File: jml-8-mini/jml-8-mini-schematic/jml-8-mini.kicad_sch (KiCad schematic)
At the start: 9 parts, among them J1 Barrel_Jack, J2 Conn_01x09_Pin, SW1 SW_DPDT_x2, U1 Z80CPU, U2 28HC64, U3 60L256, U4 Z80 CTC, U5 Z80 SIO

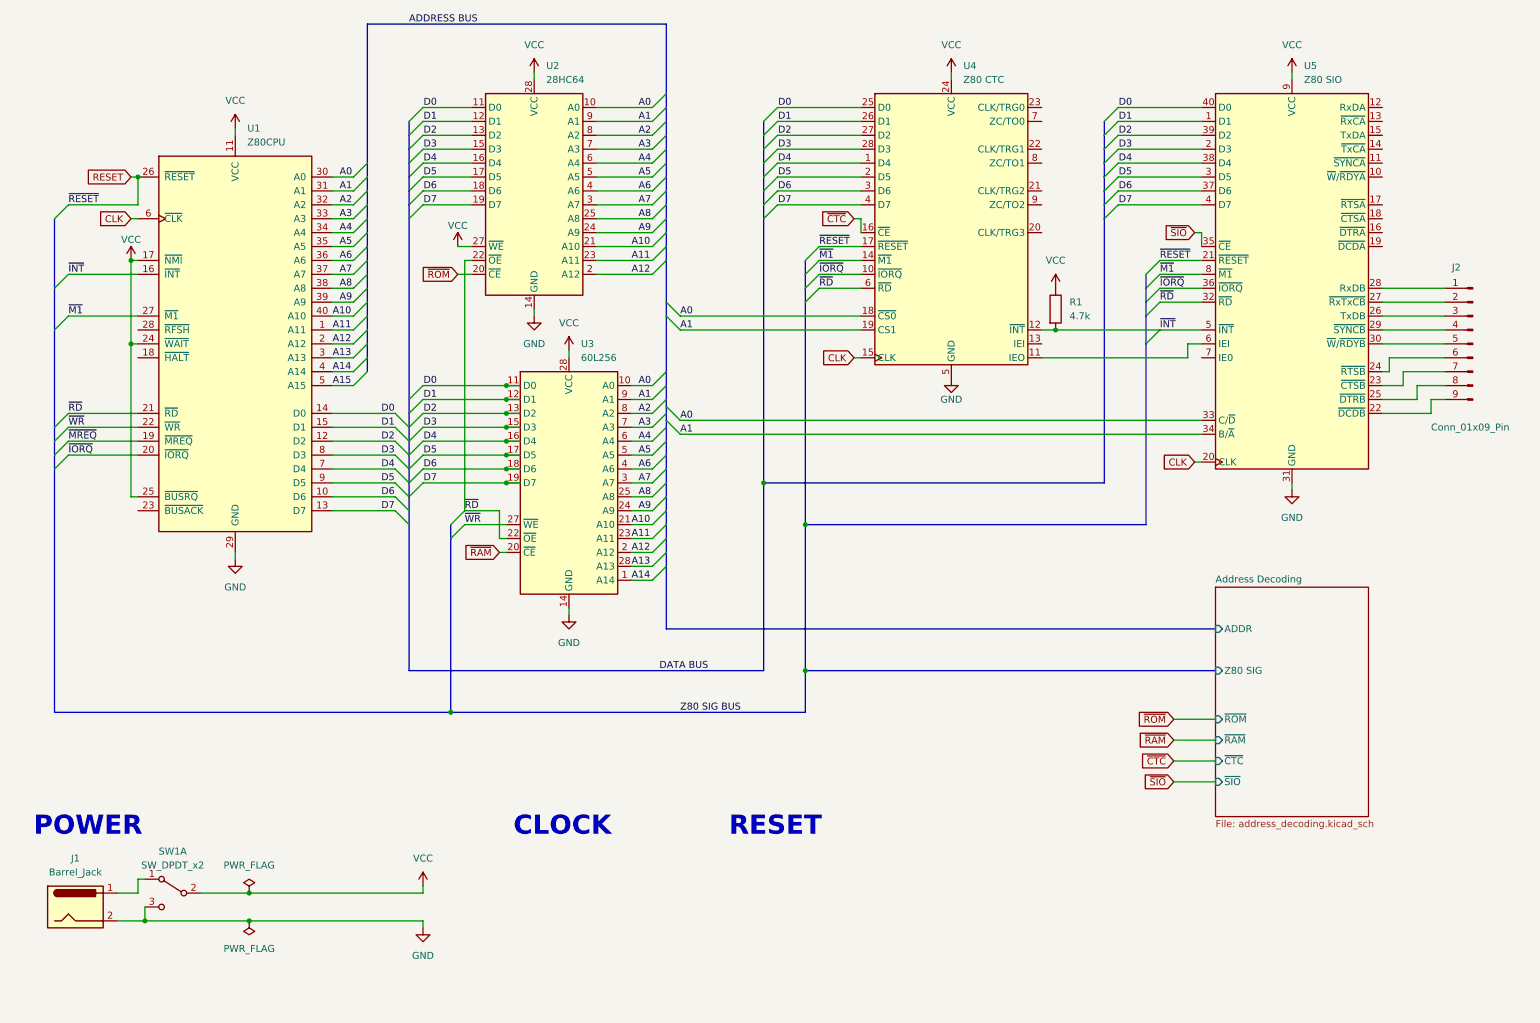
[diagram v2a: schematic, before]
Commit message: updates to jml-8 mini schematic
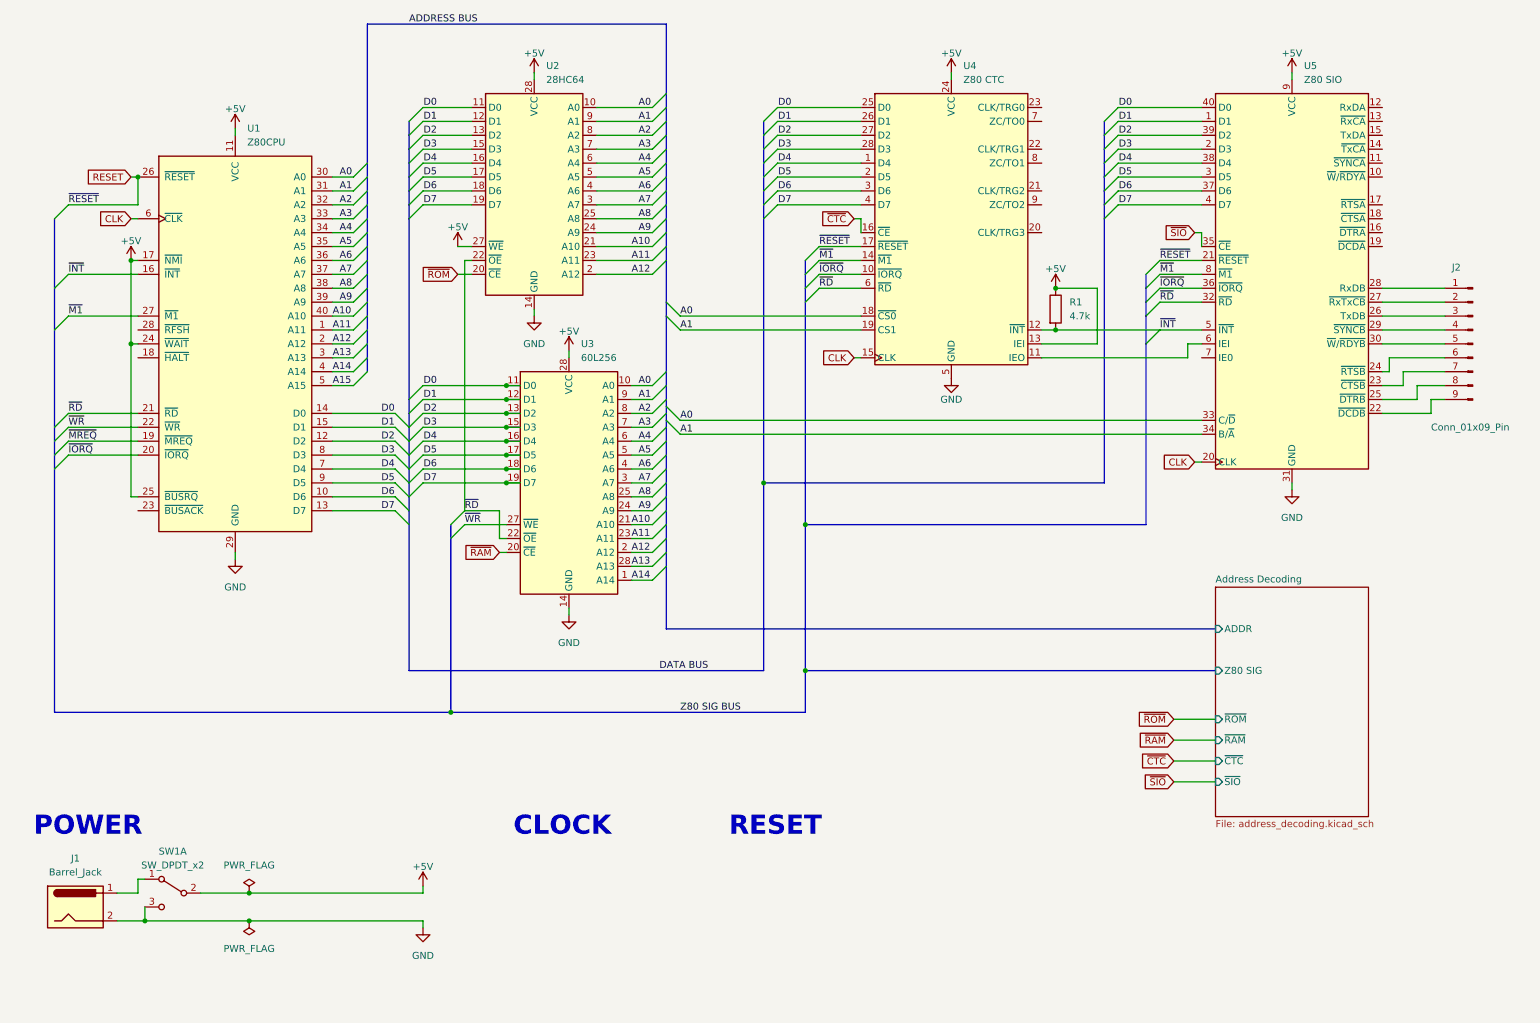
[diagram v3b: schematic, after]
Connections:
- net +5V: now reaches U4.13 (IEI)
- net +5V: now also R1.1, SW1.2 (B), U1.11 (VCC), U1.17 (~{NMI}), U1.24 (~{WAIT}), U1.25 (~{BUSRQ}), U2.27 (~{WE}), U2.28 (VCC), U3.28 (VCC), U4.24 (VCC), U5.9 (VCC)
- removed net VCC: R1.1, SW1.2 (B), U1.11 (VCC), U1.17 (~{NMI}), U1.24 (~{WAIT}), U1.25 (~{BUSRQ}), U2.27 (~{WE}), U2.28 (VCC), U3.28 (VCC), U4.24 (VCC), U5.9 (VCC)
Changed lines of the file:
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@@
   (junction (at 200.66 73.66) (diameter 0) (color 0 0 0 0)
   )
+  (junction (at 200.66 66.04) (diameter 0) (color 0 0 0 0)
+  )
   (junction (at 100.33 86.36) (diameter 0) (color 0 0 0 0)
   )
@@
     (stroke (width 0) (type default))
   )
+  (wire (pts (xy 198.12 76.2) (xy 208.28 76.2))
+    (stroke (width 0) (type default))
+  )
   (bus (pts (xy 74.93 66.04) (xy 74.93 63.5))
     (stroke (width 0) (type default))
@@
     (stroke (width 0) (type default))
   )
+  (wire (pts (xy 208.28 76.2) (xy 208.28 66.04))
+    (stroke (width 0) (type default))
+  )
   (wire (pts (xy 68.58 101.6) (xy 80.01 101.6))
     (stroke (width 0) (type default))
@@
   )
   (bus (pts (xy 74.93 68.58) (xy 74.93 66.04))
+    (stroke (width 0) (type default))
+  )
+  (wire (pts (xy 208.28 66.04) (xy 200.66 66.04))
     (stroke (width 0) (type default))
   )
@@
     )
   )
-  (symbol (lib_id "power:VCC") (at 243.84 26.67 0) (unit 1)
+  (symbol (lib_id "power:+5V") (at 243.84 26.67 0) (unit 1)
     (in_bom yes) (on_board yes) (dnp no) (fields_autoplaced)
-    (property "Reference" "#PWR06" (at 243.84 30.48 0)
-      (effects (font (size 1.27 1.27)) hide)
-    )
-    (property "Value" "VCC" (at 243.84 21.59 0)
+    (property "Reference" "#PWR?" (at 243.84 30.48 0)
+      (effects (font (size 1.27 1.27)) hide)
+    )
+    (property "Value" "+5V" (at 243.84 23.114 0)
       (effects (font (size 1.27 1.27)))
     )
@@
       (project "jml-8-mini"
         (path "/7f93abb4-2372-4a9e-a664-5edb67349db4"
-          (reference "#PWR06") (unit 1)
+          (reference "#PWR?") (unit 1)
         )
       )
@@
     )
   )
-  (symbol (lib_id "power:VCC") (at 85.09 175.26 0) (unit 1)
+  (symbol (lib_id "power:+5V") (at 85.09 175.26 0) (unit 1)
     (in_bom yes) (on_board yes) (dnp no) (fields_autoplaced)
-    (property "Reference" "#PWR01" (at 85.09 179.07 0)
-      (effects (font (size 1.27 1.27)) hide)
-    )
-    (property "Value" "VCC" (at 85.09 170.18 0)
+    (property "Reference" "#PWR?" (at 85.09 179.07 0)
+      (effects (font (size 1.27 1.27)) hide)
+    )
+    (property "Value" "+5V" (at 85.09 171.704 0)
       (effects (font (size 1.27 1.27)))
     )
@@
       (project "jml-8-mini"
         (path "/7f93abb4-2372-4a9e-a664-5edb67349db4"
-          (reference "#PWR01") (unit 1)
+          (reference "#PWR?") (unit 1)
         )
       )
@@
     )
   )
-  (symbol (lib_id "power:VCC") (at 200.66 66.04 0) (unit 1)
+  (symbol (lib_id "power:+5V") (at 200.66 66.04 0) (unit 1)
     (in_bom yes) (on_board yes) (dnp no) (fields_autoplaced)
-    (property "Reference" "#PWR017" (at 200.66 69.85 0)
-      (effects (font (size 1.27 1.27)) hide)
-    )
-    (property "Value" "VCC" (at 200.66 60.96 0)
+    (property "Reference" "#PWR?" (at 200.66 69.85 0)
+      (effects (font (size 1.27 1.27)) hide)
+    )
+    (property "Value" "+5V" (at 200.66 62.484 0)
       (effects (font (size 1.27 1.27)))
     )
@@
       (project "jml-8-mini"
         (path "/7f93abb4-2372-4a9e-a664-5edb67349db4"
-          (reference "#PWR017") (unit 1)
+          (reference "#PWR?") (unit 1)
         )
       )
@@
     )
   )
-  (symbol (lib_id "power:VCC") (at 111.76 77.47 0) (unit 1)
+  (symbol (lib_id "power:+5V") (at 111.76 77.47 0) (unit 1)
     (in_bom yes) (on_board yes) (dnp no) (fields_autoplaced)
-    (property "Reference" "#PWR07" (at 111.76 81.28 0)
-      (effects (font (size 1.27 1.27)) hide)
-    )
-    (property "Value" "VCC" (at 111.76 72.39 0)
+    (property "Reference" "#PWR?" (at 111.76 81.28 0)
+      (effects (font (size 1.27 1.27)) hide)
+    )
+    (property "Value" "+5V" (at 111.76 73.914 0)
       (effects (font (size 1.27 1.27)))
     )
@@
       (project "jml-8-mini"
         (path "/7f93abb4-2372-4a9e-a664-5edb67349db4"
-          (reference "#PWR07") (unit 1)
+          (reference "#PWR?") (unit 1)
         )
       )
@@
     )
   )
-  (symbol (lib_id "power:VCC") (at 91.44 58.42 0) (unit 1)
+  (symbol (lib_id "power:+5V") (at 91.44 58.42 0) (unit 1)
     (in_bom yes) (on_board yes) (dnp no)
-    (property "Reference" "#PWR013" (at 91.44 62.23 0)
-      (effects (font (size 1.27 1.27)) hide)
-    )
-    (property "Value" "VCC" (at 91.44 54.61 0)
+    (property "Reference" "#PWR?" (at 91.44 62.23 0)
+      (effects (font (size 1.27 1.27)) hide)
+    )
+    (property "Value" "+5V" (at 91.44 54.864 0)
       (effects (font (size 1.27 1.27)))
     )
@@
       (project "jml-8-mini"
         (path "/7f93abb4-2372-4a9e-a664-5edb67349db4"
-          (reference "#PWR013") (unit 1)
+          (reference "#PWR?") (unit 1)
         )
       )
@@
     )
   )
-  (symbol (lib_id "power:VCC") (at 105.41 26.67 0) (unit 1)
+  (symbol (lib_id "power:+5V") (at 105.41 26.67 0) (unit 1)
     (in_bom yes) (on_board yes) (dnp no) (fields_autoplaced)
-    (property "Reference" "#PWR04" (at 105.41 30.48 0)
-      (effects (font (size 1.27 1.27)) hide)
-    )
-    (property "Value" "VCC" (at 105.41 21.59 0)
+    (property "Reference" "#PWR?" (at 105.41 30.48 0)
+      (effects (font (size 1.27 1.27)) hide)
+    )
+    (property "Value" "+5V" (at 105.41 23.114 0)
       (effects (font (size 1.27 1.27)))
     )
@@
       (project "jml-8-mini"
         (path "/7f93abb4-2372-4a9e-a664-5edb67349db4"
-          (reference "#PWR04") (unit 1)
+          (reference "#PWR?") (unit 1)
         )
       )
@@
     )
   )
-  (symbol (lib_id "power:VCC") (at 181.61 26.67 0) (unit 1)
+  (symbol (lib_id "power:+5V") (at 181.61 26.67 0) (unit 1)
     (in_bom yes) (on_board yes) (dnp no) (fields_autoplaced)
-    (property "Reference" "#PWR05" (at 181.61 30.48 0)
-      (effects (font (size 1.27 1.27)) hide)
-    )
-    (property "Value" "VCC" (at 181.61 21.59 0)
+    (property "Reference" "#PWR?" (at 181.61 30.48 0)
+      (effects (font (size 1.27 1.27)) hide)
+    )
+    (property "Value" "+5V" (at 181.61 23.114 0)
       (effects (font (size 1.27 1.27)))
     )
@@
       (project "jml-8-mini"
         (path "/7f93abb4-2372-4a9e-a664-5edb67349db4"
-          (reference "#PWR05") (unit 1)
-        )
-      )
-    )
-  )
-  (symbol (lib_id "power:VCC") (at 50.8 36.83 0) (unit 1)
+          (reference "#PWR?") (unit 1)
+        )
+      )
+    )
+  )
+  (symbol (lib_id "power:+5V") (at 50.8 36.83 0) (unit 1)
     (in_bom yes) (on_board yes) (dnp no) (fields_autoplaced)
-    (property "Reference" "#PWR03" (at 50.8 40.64 0)
-      (effects (font (size 1.27 1.27)) hide)
-    )
-    (property "Value" "VCC" (at 50.8 31.75 0)
+    (property "Reference" "#PWR?" (at 50.8 40.64 0)
+      (effects (font (size 1.27 1.27)) hide)
+    )
+    (property "Value" "+5V" (at 50.8 33.274 0)
       (effects (font (size 1.27 1.27)))
     )
@@
       (project "jml-8-mini"
         (path "/7f93abb4-2372-4a9e-a664-5edb67349db4"
-          (reference "#PWR03") (unit 1)
+          (reference "#PWR?") (unit 1)
         )
       )
@@
     )
   )
-  (symbol (lib_id "power:VCC") (at 31.75 60.96 0) (unit 1)
+  (symbol (lib_id "power:+5V") (at 31.75 60.96 0) (unit 1)
     (in_bom yes) (on_board yes) (dnp no)
-    (property "Reference" "#PWR014" (at 31.75 64.77 0)
-      (effects (font (size 1.27 1.27)) hide)
-    )
-    (property "Value" "VCC" (at 31.75 57.15 0)
+    (property "Reference" "#PWR?" (at 31.75 64.77 0)
+      (effects (font (size 1.27 1.27)) hide)
+    )
+    (property "Value" "+5V" (at 31.75 57.404 0)
       (effects (font (size 1.27 1.27)))
     )
@@
       (project "jml-8-mini"
         (path "/7f93abb4-2372-4a9e-a664-5edb67349db4"
-          (reference "#PWR014") (unit 1)
-        )
-      )
+          (reference "#PWR?") (unit 1)
+        )
+      )

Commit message: updates to schematics
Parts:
- added J3: Conn_01x04_Pin, symbol Connector:Conn_01x04_Pin
- added R10, R2, R6, R7, R8, R9: 10K, symbol Device:R_Small
- added R3, R4, R5: 2K7, symbol Device:R_Small
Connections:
- net +5V: now also R10.1, R2.1, R6.1, R7.1, R8.1, R9.1; no longer U1.17 (~{NMI}), U1.24 (~{WAIT}), U1.25 (~{BUSRQ}), U2.27 (~{WE}), U4.13 (IEI)
- net GND: now also U5.18 (~{CTSA}), U5.19 (~{DCDA}), J3.4 (Pin_4)
- net at U4.7 (ZC/TO0): now also U5.13 (~{RxCA}), U5.14 (~{TxCA})
- net at U5.11 (~{SYNCA}): now also R2.2
- net at U5.12 (RxDA): now also R4.2
- net at U5.15 (TxDA): now also R3.2
- net at U5.17 (~{RTSA}): now also R5.2
- new net: R7.2, U2.27 (~{WE})
- new net: R6.2, U4.13 (IEI)
- new net: J3.1 (Pin_1), R3.1
- new net: J3.2 (Pin_2), R4.1
- new net: J3.3 (Pin_3), R5.1
- new net: R8.2, U1.17 (~{NMI})
- new net: R9.2, U1.24 (~{WAIT})
- new net: R10.2, U1.25 (~{BUSRQ})

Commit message: many changes to schematic to make more organized
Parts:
- removed J2: Conn_01x09_Pin, symbol Connector:Conn_01x09_Pin
- removed J3: Conn_01x04_Pin, symbol Connector:Conn_01x04_Pin
- removed R1: 4.7k, symbol Device:R
- removed R10, R2, R6, R7, R8, R9: 10K, symbol Device:R_Small
- removed R3, R4, R5: 2K7, symbol Device:R_Small
- removed U2: 28HC64, Package_DIP:DIP-28_W15.24mm_LongPads, symbol jml-8-mini-library:AT28HC64B
- removed U3: 60L256, Package_DIP:DIP-28_W15.24mm_LongPads, symbol jml-8-mini-library:MCM60L256AP85
- removed U4: Z80 CTC, symbol jml-8-mini-library:Z80_CTC
- removed U5: Z80 SIO, symbol jml-8-mini-library:Z80_SIO/0
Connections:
- net CLK renamed Clock and Reset/CLK
- net RESET renamed ~{RESET}
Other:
- added sheet Clock and Reset (clock_reset.kicad_sch)
- added sheet Memory (memory.kicad_sch)
- added sheet Peripherals (peripherals.kicad_sch)
- sheet Address Decoding ports: added ADDR BUS, Z80 SIG BUS; removed ADDR, Z80 SIG
- note added: "CHIP SELECT"
- note added: "CLOCK RESET"
- note added: "MEMORY"
- note added: "PERIPHERALS"
- note removed: "CLOCK"
- note removed: "RESET"
- moved on the sheet: U1
